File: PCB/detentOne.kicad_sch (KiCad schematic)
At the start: 8 parts, among them SW7 C92589, SW8 C92589, U3 ESP32-S3-WROOM-1(N16R8)

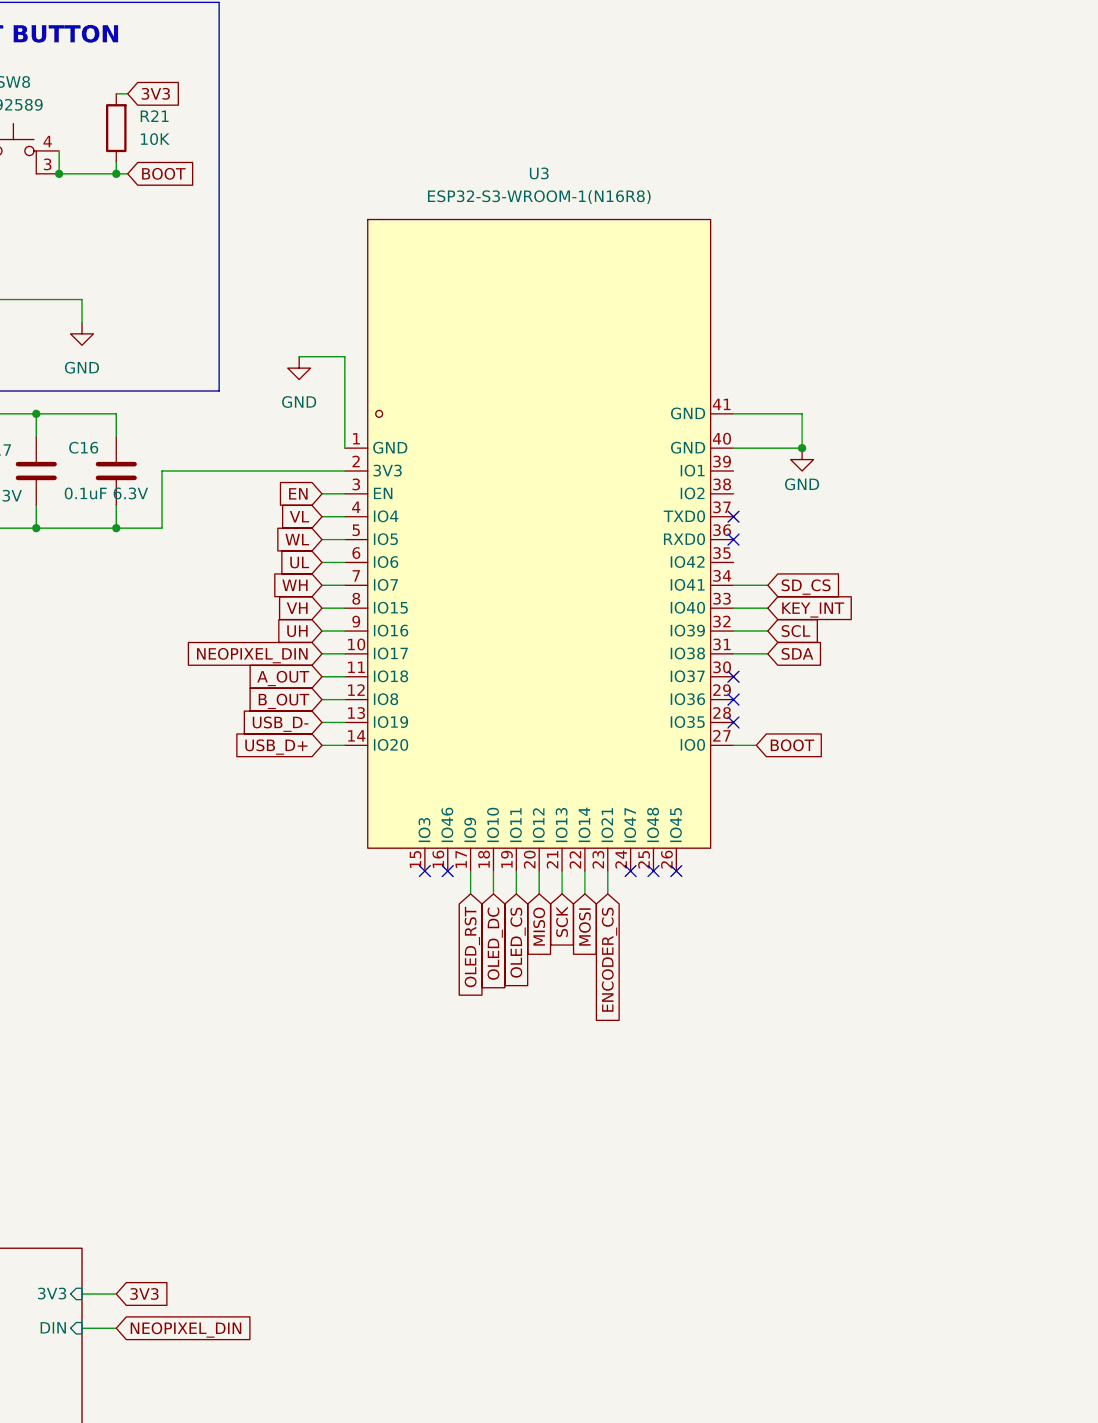
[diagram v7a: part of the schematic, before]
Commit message: silkscreen done
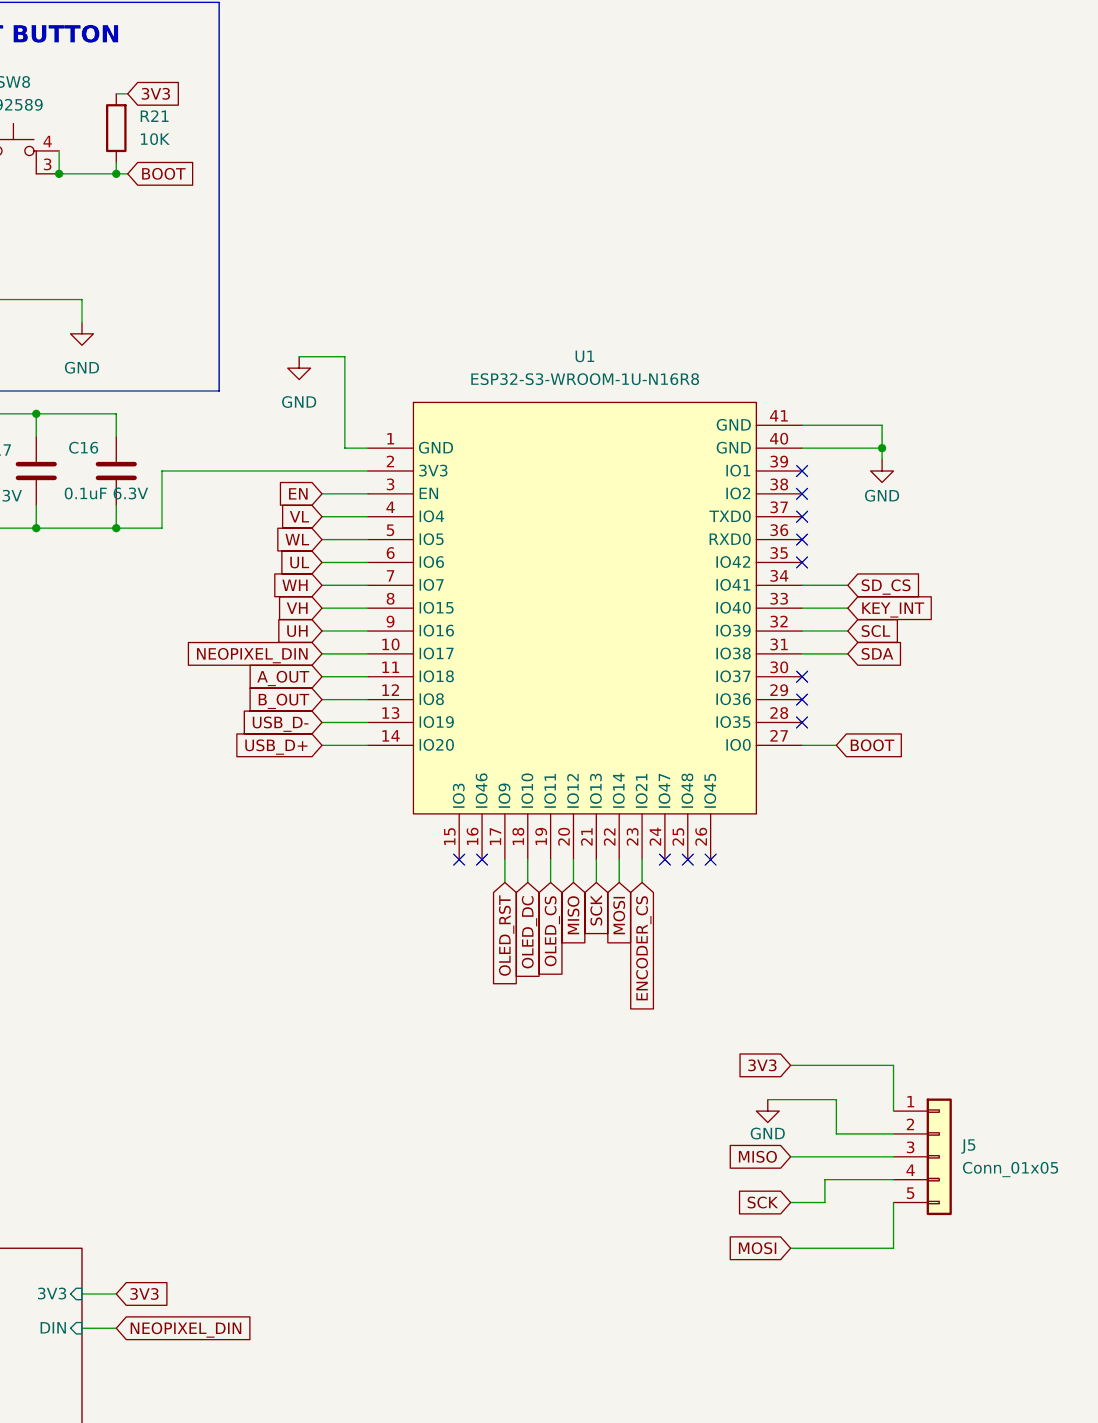
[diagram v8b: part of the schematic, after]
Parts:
- removed U3: ESP32-S3-WROOM-1(N16R8), easyeda2kicad:WIRELM-SMD_ESP32-S3-WROOM-1, symbol easyeda2kicad:ESP32-S3-WROOM-1(N16R8)
- added J5: Conn_01x05, Connector_PinHeader_2.54mm:PinHeader_1x05_P2.54mm_Vertical, symbol Connector_Generic:Conn_01x05
- added U1: ESP32-S3-WROOM-1U-N16R8, easyeda2kicad:WIRELM-SMD_ESP32-S3-WROOM-1U, symbol easyeda2kicad:ESP32-S3-WROOM-1U-N16R8
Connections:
- net 3V3: now also J5.1 (Pin_1), U1.2 (3V3)
- net A_OUT: now also U1.11 (IO18)
- net BOOT: now also U1.27 (IO0)
- net B_OUT: now also U1.12 (IO8)
- net EN: now also U1.3 (EN)
- net ENCODER_CS: now also U1.23 (IO21)
- net GND: now also J5.2 (Pin_2), U1.1 (GND), U1.40 (GND), U1.41 (GND)
- net KEY_INT: now also U1.33 (IO40)
- net MISO: now also J5.3 (Pin_3), U1.20 (IO12)
- net MOSI: now also J5.5 (Pin_5), U1.22 (IO14)
- net NEOPIXEL_DIN: now also U1.10 (IO17)
- net OLED_CS: now also U1.19 (IO11)
- net OLED_DC: now also U1.18 (IO10)
- net OLED_RST: now also U1.17 (IO9)
- net SCK: now also J5.4 (Pin_4), U1.21 (IO13)
- net SCL: now also U1.32 (IO39)
- net SDA: now also U1.31 (IO38)
- net SD_CS: now also U1.34 (IO41)
- net UH: now also U1.9 (IO16)
- net UL: now also U1.6 (IO6)
- net USB_D+: now also U1.14 (IO20)
- net USB_D-: now also U1.13 (IO19)
- net VH: now also U1.8 (IO15)
- net VL: now also U1.4 (IO4)
- net WH: now also U1.7 (IO7)
- net WL: now also U1.5 (IO5)
- no-connect marks 10 -> 13
